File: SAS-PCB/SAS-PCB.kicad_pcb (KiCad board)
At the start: 2 copper layers, 164 x 88 mm, 23 parts, among them J1-BMP280 Conn_01x06_Pin, J2 Conn_02x20_Odd_Even, J3-GPS1 Conn_01x04_Socket, J4-LCD1 Conn_01x04_Socket, J4-LCD2 Conn_01x04_Socket, J5_Batt1 691137710002

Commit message: Rooting terminé
Reste à refaire les mounting holes et enlever les bouttes de cuivre trop mince.
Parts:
- removed Fan_1, Fan_2: 691137710002, SAS-Librarie-Empreinte:bornie_2position
- added J8-Fan1: Conn_01x04_Socket, SAS-Librarie-Empreinte:Conn_4_pos, F.Cu at (182.1, 52.2)
- added J9-Fan2: Conn_01x04_Socket, SAS-Librarie-Empreinte:Conn_4_pos, F.Cu at (182.1, 36.8)
- J4-BMP280: renamed from J1-BMP280; footprint SAS-Librarie-Empreinte:Conn_6_pos -> SAS-Librarie-Empreinte:Header-BMP280
- J5-GPS1: renamed from J3-GPS1; footprint SAS-Librarie-Empreinte:Conn_4_pos -> SAS-Librarie-Empreinte:conn-GPS
- moved Bouton_6 122.4 mm to (134.0, 109.5), turned to 180 degrees
- moved J4-BMP280 114.0 mm to (144.5, 68.9), turned to 180 degrees
- moved J3-LCD2 103.6 mm to (191.2, 82.3)
- moved Bouton_5 99.6 mm to (145.5, 109.5), turned to 180 degrees
- moved R6 98.7 mm to (141.3, 102.5), turned to 90 degrees
- moved Bouton_1 94.9 mm to (191.5, 109.5), turned to 180 degrees
- moved Bouton_4 83.6 mm to (157.0, 109.5), turned to 180 degrees
- moved R1 81.6 mm to (194.0, 97.5), turned to -90 degrees
- moved J1_Batt1 81.6 mm to (203.0, 62.5), turned to 90 degrees
- moved Bouton_2 79.5 mm to (180.0, 109.5), turned to 180 degrees
- moved J5-GPS1 77.4 mm to (143.5, 49.0), turned to 180 degrees
- moved Bouton_3 75.8 mm to (168.5, 109.5), turned to 180 degrees
- moved R5 74.9 mm to (152.8, 102.5), turned to 90 degrees
- moved R7 71.2 mm to (165.2, 68.0), turned to -90 degrees
- moved J2-LCD1 66.6 mm to (172.8, 82.3)
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- renumbered J5_Batt1 to J1_Batt1, J4-LCD1 to J2-LCD1, J4-LCD2 to J3-LCD2, J2 to J6-cable-plat1, RFD900x1 to J7-RFD900x1
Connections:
- J6-cable-plat1 pad 12: unconnected-(J2-Pin_12-Pad12) -> Fan1_PWM
- J6-cable-plat1 pad 13: unconnected-(J2-Pin_13-Pad13) -> Fan2_PWM
- J6-cable-plat1 pad 22: unconnected-(J2-Pin_22-Pad22) -> Fan1_RPM
- J6-cable-plat1 pad 24: unconnected-(J2-Pin_24-Pad24) -> Fan2_RPM
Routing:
- net Fan2_RPM: track 0.00 -> 115.2 mm
- net Fan1_RPM: track 0.00 -> 110.9 mm
- net Fan1_PWM: track 0.00 -> 93.0 mm
- net SDA: track 0.00 -> 90.3 mm
- net SCL: track 0.00 -> 88.8 mm
- net Bouton_1: track 0.00 -> 72.4 mm
- net Fan2_PWM: track 0.00 -> 62.7 mm
- net Bouton_2: track 0.00 -> 59.9 mm
- net Bouton_3: track 0.00 -> 47.0 mm
- net RXD: track 0.00 -> 41.5 mm
- net TXD: track 0.00 -> 37.5 mm
- net Bouton_4: track 0.00 -> 34.5 mm
- net Bouton_5: track 0.00 -> 21.9 mm
- net Bouton_6: track 0.00 -> 9.39 mm
- net Net-(Bouton_5-GND): track 0.00 -> 7.87 mm
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- added copper zone on F.Cu, net +3.3V
- added copper zone on F.Cu, net +5V
- added copper zone on B.Cu, net GND
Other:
- board size 164 x 88 mm -> 96.5 x 85.5 mm
- board text added: "GAUL-SAS"

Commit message: Header Fix
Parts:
- moved J4-BMP280 1.57 mm to (144.5, 67.3)
- moved R4 0.30 mm to (164.6, 102.5)
- moved R3 0.23 mm to (176.0, 102.5)
- moved R6 0.18 mm to (141.5, 102.5)
- moved R2 0.13 mm to (182.4, 97.5)
- moved R5 0.11 mm to (152.9, 102.5)
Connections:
- J6-cable-plat1 pad 11: unconnected-(J6-cable-plat1-Pin_11-Pad11) -> Bouton_1
- J6-cable-plat1 pad 12: Fan1_PWM -> unconnected-(J6-cable-plat1-Pin_12-Pad12)
- J6-cable-plat1 pad 13: Fan2_PWM -> Bouton_2
- J6-cable-plat1 pad 15: unconnected-(J6-cable-plat1-Pin_15-Pad15) -> Bouton_3
- J6-cable-plat1 pad 16: unconnected-(J6-cable-plat1-Pin_16-Pad16) -> Fan1_RPM
- J6-cable-plat1 pad 18: unconnected-(J6-cable-plat1-Pin_18-Pad18) -> Fan2_RPM
- J6-cable-plat1 pad 22: Fan1_RPM -> unconnected-(J6-cable-plat1-Pin_22-Pad22)
- J6-cable-plat1 pad 24: Fan2_RPM -> unconnected-(J6-cable-plat1-Pin_24-Pad24)
- J6-cable-plat1 pad 27: Bouton_1 -> unconnected-(J6-cable-plat1-Pin_27-Pad27)
- J6-cable-plat1 pad 29: Bouton_2 -> Bouton_4
- J6-cable-plat1 pad 31: Bouton_3 -> Bouton_5
- J6-cable-plat1 pad 32: unconnected-(J6-cable-plat1-Pin_32-Pad32) -> Fan1_PWM
- J6-cable-plat1 pad 33: Bouton_4 -> Fan2_PWM
- J6-cable-plat1 pad 35: Bouton_5 -> unconnected-(J6-cable-plat1-Pin_35-Pad35)
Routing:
- net +3.3V: track 0.00 -> 35.4 mm
- net Bouton_1: track 72.4 -> 91.6 mm
- net Bouton_2: track 59.9 -> 78.7 mm
- net Bouton_3: track 47.0 -> 65.8 mm
- net Fan2_PWM: track 62.7 -> 80.8 mm
- net Fan1_PWM: track 93.0 -> 105.5 mm
- net Fan1_RPM: track 110.9 -> 102.8 mm
- net Fan2_RPM: track 115.2 -> 107.5 mm
- net Bouton_4: track 34.5 -> 36.8 mm
- net Bouton_5: track 21.9 -> 24.0 mm
- net RXD: track 41.5 -> 42.6 mm

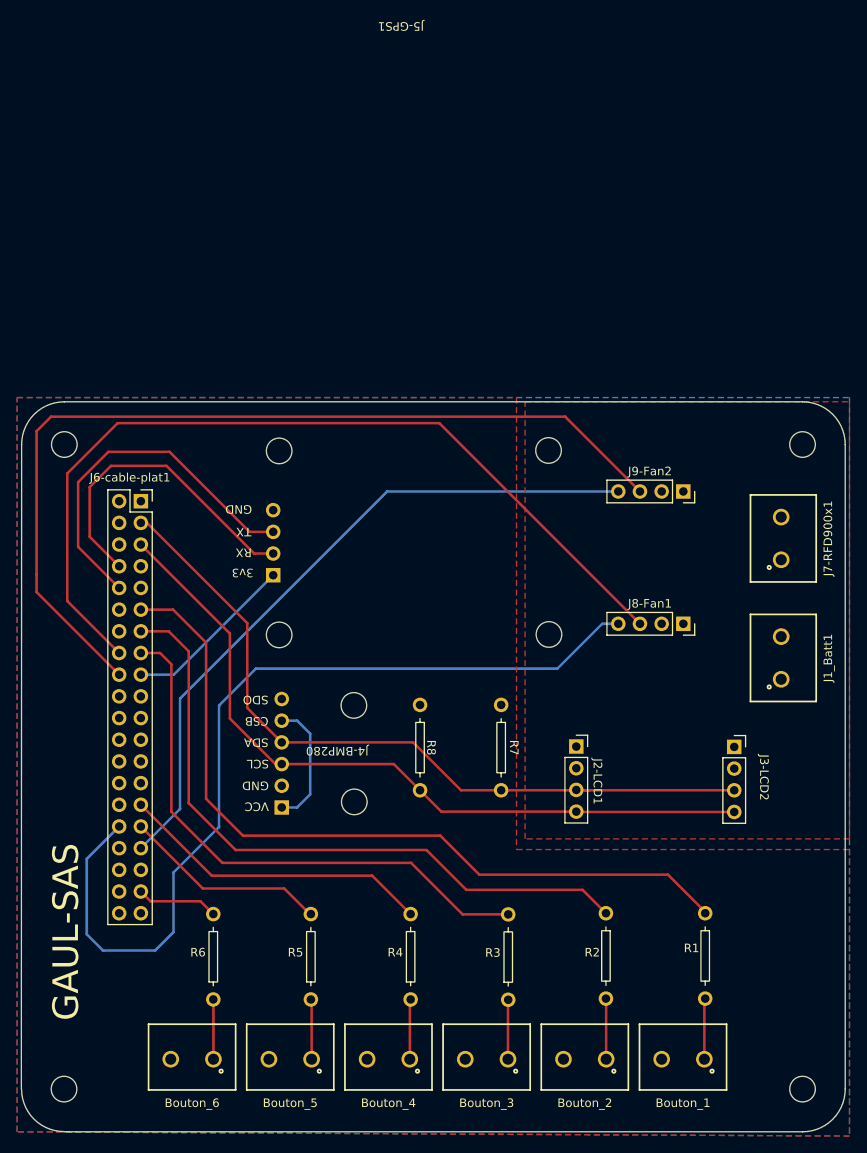
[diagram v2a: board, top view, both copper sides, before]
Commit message: Modification des power plane, corrections DRC et extraction des fichiers gerber
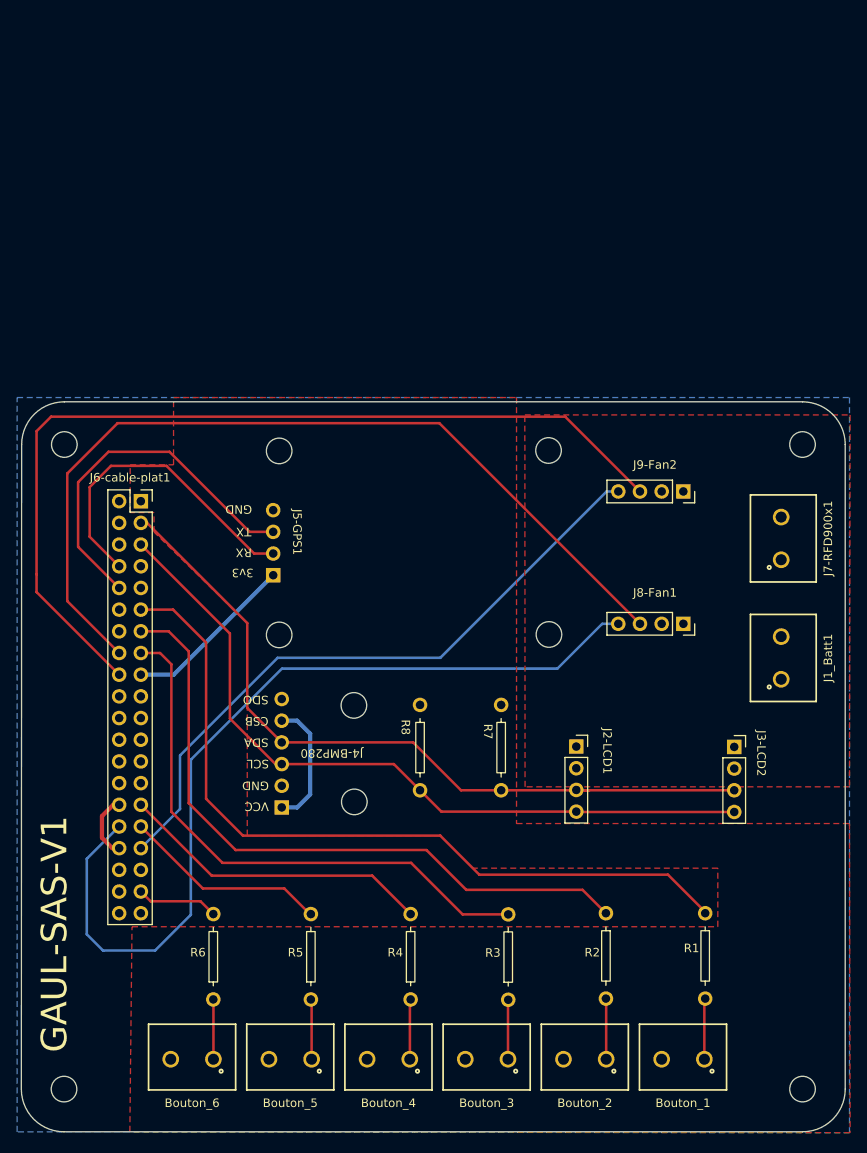
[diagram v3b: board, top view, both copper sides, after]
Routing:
- net GND: track 0.00 -> 7.62 mm
- net Fan2_PWM: track 80.8 -> 76.9 mm
- net Fan1_PWM: track 105.5 -> 103.7 mm
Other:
- board text added: "GAUL-SAS-V1"
- board text removed: "GAUL-SAS"
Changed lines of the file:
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@@
 			(outputformat 1)
 			(mirror no)
-			(drillshape 1)
+			(drillshape 0)
 			(scaleselection 1)
-			(outputdirectory "")
+			(outputdirectory "./")
 		)
 	)
@@
 		(at 143.5 49 180)
 		(property "Reference" "J5-GPS1"
-			(at -14.96 60.5 180)
+			(at -2.804 1.248 -90)
 			(unlocked yes)
 			(layer "F.SilkS")
@@
 			)
 		)
-		(fp_text user "${REFERENCE}"
-			(at -14.96 63.5 180)
-			(unlocked yes)
-			(layer "F.Fab")
-			(effects
-				(font
-					(size 1 1)
-					(thickness 0.15)
-				)
-			)
-		)
 		(pad "1" thru_hole rect
 			(at 0 -3.81 180)
@@
 		(at 172.75 82.28)
 		(property "Reference" "J2-LCD1"
-			(at 8.75 -5.32 -90)
+			(at 9.876 -8.874 -90)
 			(unlocked yes)
 			(layer "F.SilkS")
@@
 		(at 165.2 68 -90)
 		(property "Reference" "R7"
-			(at 5 -6.5 -90)
+			(at 3.12 -3.456 -90)
 			(unlocked yes)
 			(layer "F.SilkS")
@@
 		(at 144.5 67.31 180)
 		(property "Reference" "J4-BMP280"
-			(at -6.5 -6.08 180)
+			(at -5.868 -6.35 180)
 			(unlocked yes)
 			(layer "F.SilkS")
@@
 		(at 191.25 82.32)
 		(property "Reference" "J3-LCD2"
-			(at 9.75 -5.82 -90)
+			(at 9.41 -8.66 -90)
 			(unlocked yes)
 			(layer "F.SilkS")
@@
 		(at 155.7 68 -90)
 		(property "Reference" "R8"
-			(at 5 -6.3 -90)
+			(at 2.612 -3.304 -90)
 			(unlocked yes)
 			(layer "F.SilkS")
@@
 		(at 182.14 36.75 -90)
 		(property "Reference" "J9-Fan2"
-			(at 3.8875 -5.4875 0)
+			(at 3.128 -6.074 0)
 			(unlocked yes)
 			(layer "F.SilkS")
@@
 		(at 182.14 52.25 -90)
 		(property "Reference" "J8-Fan1"
-			(at 3.8875 -5.4875 0)
+			(at 2.614 -6.074 0)
 			(unlocked yes)
 			(layer "F.SilkS")
@@
 	)
 	(gr_arc
-		(start 119 117.974937)
-		(mid 115.482188 116.517812)
-		(end 114.025063 113)
+		(start 119 118)
+		(mid 115.464466 116.535534)
+		(end 114 113)
 		(stroke
 			(width 0.05)
@@
 		(stroke
 			(width 0.05)
-			(type default)
+			(type solid)
 		)
 		(fill none)
@@
 		(layer "Edge.Cuts")
 	)
-	(gr_text "GAUL-SAS"
-		(at 121 105 90)
+	(gr_text "GAUL-SAS-V1"
+		(at 119.634 108.712 90)
 		(layer "F.SilkS")
 		(effects
 			(font
 				(size 3 3)
-				(thickness 0.1)
+				(thickness 0.3)
 			)
 			(justify left bottom)
@@
 		(start 147.828 71.374)
 		(end 146.304 69.85)
-		(width 0.3)
+		(width 0.5)
 		(layer "B.Cu")
 		(net 2)
@@
 		(start 146.304 80.01)
 		(end 147.828 78.486)
-		(width 0.3)
+		(width 0.5)
 		(layer "B.Cu")
 		(net 2)
@@
 		(start 144.5 80.01)
 		(end 146.304 80.01)
-		(width 0.3)
+		(width 0.5)
 		(layer "B.Cu")
 		(net 2)
@@
 		(start 147.828 78.486)
 		(end 147.828 71.374)
-		(width 0.3)
+		(width 0.5)
 		(layer "B.Cu")
 		(net 2)
@@
 		(start 146.304 69.85)
 		(end 144.5 69.85)
-		(width 0.3)
+		(width 0.5)
 		(layer "B.Cu")
 		(net 2)
@@
 		(start 131.85 64.46)
 		(end 143.5 52.81)
-		(width 0.3)
+		(width 0.5)
 		(layer "B.Cu")
 		(net 2)
@@
 		(start 128 64.46)
 		(end 131.85 64.46)
-		(width 0.3)
+		(width 0.5)
 		(layer "B.Cu")
 		(net 2)
@@
 	)
 	(segment
+		(start 123.444 81.026)
+		(end 124.77 79.7)
+		(width 0.5)
+		(layer "F.Cu")
+		(net 9)
+	)
+	(segment
+		(start 124.77 79.7)
+		(end 125.46 79.7)
+		(width 0.5)
+		(layer "F.Cu")
+		(net 9)
+	)
+	(segment
+		(start 125.46 84.78)
+		(end 124.658 84.78)
+		(width 0.5)
+		(layer "F.Cu")
+		(net 9)
+	)
+	(segment
+		(start 124.658 84.78)
+		(end 123.444 83.566)
+		(width 0.5)
+		(layer "F.Cu")
+		(net 9)
+	)
+	(segment
+		(start 123.444 83.566)
+		(end 123.444 81.026)
+		(width 0.5)
+		(layer "F.Cu")
+		(net 9)
+	)
+	(segment
 		(start 144.5 74.93)
 		(end 143.764 74.93)
@@
 	)
 	(segment
-		(start 132.588 67.263585)
-		(end 132.588 80.192)
+		(start 183.92 43)
+		(end 182.552 43)
 		(width 0.3)
 		(layer "B.Cu")
@@
 	)
 	(segment
-		(start 141.019877 58.831708)
-		(end 132.588 67.263585)
+		(start 132.588 80.192)
+		(end 128 84.78)
 		(width 0.3)
 		(layer "B.Cu")
@@
 	)
 	(segment
-		(start 156.851584 43)
-		(end 141.019877 58.831708)
+		(start 132.588 73.914)
+		(end 132.588 80.192)
 		(width 0.3)
 		(layer "B.Cu")
@@
 	)
 	(segment
-		(start 183.92 43)
-		(end 156.851584 43)
+		(start 144.018 62.484)
+		(end 132.588 73.914)
 		(width 0.3)
 		(layer "B.Cu")
@@
 	)
 	(segment
-		(start 132.588 80.192)
-		(end 128 84.78)
+		(start 163.068 62.484)
+		(end 144.018 62.484)
+		(width 0.3)
+		(layer "B.Cu")
+		(net 18)
+	)
+	(segment
+		(start 182.552 43)
+		(end 163.068 62.484)
 		(width 0.3)
 		(layer "B.Cu")
@@
 	)
 	(segment
-		(start 183.92 58.5)
-		(end 182.038 58.5)
-		(width 0.3)
-		(layer "B.Cu")
-		(net 22)
-	)
-	(segment
-		(start 129.667 96.774)
-		(end 123.571 96.774)
+		(start 182.038 58.5)
+		(end 176.784 63.754)
 		(width 0.3)
 		(layer "B.Cu")
@@
 	)
 	(segment
-		(start 176.784 63.754)
-		(end 141.478 63.754)
+		(start 144.526 63.754)
+		(end 133.858 74.422)
 		(width 0.3)
 		(layer "B.Cu")
@@
 	)
 	(segment
-		(start 137.16 68.072)
-		(end 137.16 82.296)
-		(width 0.3)
-		(layer "B.Cu")
-		(net 22)
-	)
-	(segment
-		(start 141.478 63.754)
-		(end 137.16 68.072)
+		(start 129.667 96.774)
+		(end 123.571 96.774)
 		(width 0.3)
 		(layer "B.Cu")
@@
 	)
 	(segment
-		(start 182.038 58.5)
-		(end 176.784 63.754)
+		(start 183.92 58.5)
+		(end 182.038 58.5)
 		(width 0.3)
 		(layer "B.Cu")
@@
 	)
 	(segment
-		(start 121.666 94.869)
-		(end 121.666 86.034)
+		(start 121.666 86.034)
+		(end 125.46 82.24)
 		(width 0.3)
 		(layer "B.Cu")
@@
 	)
 	(segment
-		(start 121.666 86.034)
-		(end 125.46 82.24)
+		(start 133.858 92.583)
+		(end 129.667 96.774)
 		(width 0.3)
 		(layer "B.Cu")
@@
 	)
 	(segment
-		(start 137.16 82.296)
-		(end 131.826 87.63)
+		(start 121.666 94.869)
+		(end 121.666 86.034)
 		(width 0.3)
 		(layer "B.Cu")
@@
 	)
 	(segment
-		(start 131.826 87.63)
-		(end 131.826 94.615)
+		(start 133.858 74.422)
+		(end 133.858 92.583)
 		(width 0.3)
 		(layer "B.Cu")
@@
 	)
 	(segment
-		(start 131.826 94.615)
-		(end 129.667 96.774)
+		(start 176.784 63.754)
+		(end 144.526 63.754)
 		(width 0.3)
 		(layer "B.Cu")
@@
 		(polygon
 			(pts
-				(xy 113.5 118) (xy 113.5 32) (xy 172 32) (xy 172 84.944) (xy 211 84.944) (xy 211 118.5)
+				(xy 126.708 118) (xy 126.962 93.98) (xy 140.462 93.98) (xy 195.58 93.98) (xy 195.58 87.122) (xy 166.878 87.122)
+				(xy 163.068 83.312) (xy 140.462 83.312) (xy 140.462 58.42) (xy 129.54 47.752) (xy 129.54 45.466)
+				(xy 126.746 45.466) (xy 126.746 39.878) (xy 131.826 39.878) (xy 131.826 32) (xy 172 32) (xy 172 81.896)
+				(xy 211 81.896) (xy 211.074 118.11)
 			)
 		)
@@
 		(polygon
 			(pts
-				(xy 211 32.5) (xy 211 83.69) (xy 173 83.69) (xy 173 32.5)
+				(xy 211.074 34.036) (xy 211 77.594) (xy 173 77.594) (xy 172.974 34.036)
 			)
 		)
@@
 		(polygon
 			(pts
-				(xy 113.5 32) (xy 211 32) (xy 211 118.5) (xy 113.5 118)
+				(xy 113.5 32) (xy 211 32) (xy 211 118.11) (xy 113.5 118)
 			)
 		)

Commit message: u1
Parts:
- J1_Batt1, J7-RFD900x1: footprint SAS-Librarie-Empreinte:bornie_2position -> SAS-Librarie-Empreinte:AMASS_XT30U-F_1x02_P5.0mm_Vertical
- moved J9-Fan2 143.7 mm to (58.6, 110.2), turned to 0 degrees
- moved J7-RFD900x1 141.0 mm to (65.7, 80.5)
- moved J8-Fan1 131.5 mm to (58.6, 97.2), turned to 0 degrees
- moved R1 122.6 mm to (73.0, 78.0), turned to 90 degrees
- moved R2 106.2 mm to (78.0, 78.0), turned to 90 degrees
- moved R3 96.2 mm to (83.0, 78.0)
- moved J6-cable-plat1 88.3 mm to (74.2, 114.2), turned to 90 degrees
- moved J1_Batt1 81.0 mm to (134.3, 105.4)
- moved J5-GPS1 80.5 mm to (79.5, 98.0)
- moved R4 80.4 mm to (88.0, 78.0)
- moved Bouton_1 79.3 mm to (125.5, 65.5)
- moved Bouton_2 78.2 mm to (115.3, 65.5)
- moved Bouton_3 77.2 mm to (105.1, 65.5)
- moved Bouton_4 76.1 mm to (94.9, 65.5)
- moved Bouton_5 75.1 mm to (84.7, 65.5)
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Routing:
- net Fan2_RPM: track 107.5 -> 0.00 mm
- net Fan1_PWM: track 103.7 -> 0.00 mm
- net Fan1_RPM: track 102.8 -> 0.00 mm
- net Bouton_1: track 91.6 -> 0.00 mm
- net SDA: track 89.8 -> 0.00 mm
- net SCL: track 88.4 -> 0.00 mm
- net Bouton_2: track 78.7 -> 0.00 mm
- net Fan2_PWM: track 76.9 -> 0.00 mm
- net Bouton_3: track 65.8 -> 0.00 mm
- net RXD: track 42.6 -> 0.00 mm
- net TXD: track 37.5 -> 0.00 mm
- net Bouton_4: track 36.8 -> 0.00 mm
- net +3.3V: track 35.4 -> 0.00 mm
- net Bouton_5: track 24.0 -> 0.00 mm
- net Bouton_6: track 9.58 -> 0.00 mm
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- removed copper zone on F.Cu, net +3.3V
- removed copper zone on F.Cu, net +5V
- removed copper zone on B.Cu, net GND
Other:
- board size 96.5 x 85.5 mm -> 80 x 60 mm
- board text removed: "GAUL-SAS-V1"

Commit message: U2
trial 2
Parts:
- added J10-FTDI1: Conn_01x06, SAS-Librarie-Empreinte:Conn_6_pos, F.Cu at (65.4, 129.0)
- added J11-Conn_RFD900: Conn_01x08, SAS-Librarie-Empreinte:Conn_8_pos, F.Cu at (131.4, 120.7)
- moved J7-RFD900x1 77.6 mm to (130.4, 123.3), turned to 180 degrees
- moved J1_Batt1 69.4 mm to (64.9, 104.0), turned to 0 degrees
- moved J2-LCD1 68.4 mm to (59.9, 84.1)
- moved J9-Fan2 68.2 mm to (125.0, 94.6)
- moved J8-Fan1 68.2 mm to (125.2, 82.7)
- moved J3-LCD2 56.6 mm to (72.0, 87.2), turned to 180 degrees
- moved Bouton_1 51.8 mm to (73.7, 66.4), turned to 0 degrees
- moved Bouton_6 49.2 mm to (123.7, 66.4), turned to 0 degrees
- moved J4-BMP280 42.2 mm to (91.8, 117.9)
- moved J5-GPS1 36.3 mm to (114.2, 87.4), turned to 0 degrees
- moved Bouton_2 31.6 mm to (83.7, 66.4), turned to 0 degrees
- moved Bouton_5 29.0 mm to (113.7, 66.4), turned to 0 degrees
- moved J6-cable-plat1 16.9 mm to (75.3, 131.1)
- moved Bouton_3 11.4 mm to (93.7, 66.4), turned to 0 degrees
- moved R1 9.86 mm to (78.1, 86.5)
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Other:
- board size 80 x 60 mm -> 76.2 x 76.2 mm

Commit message: Version_a_amiliorer
pas tant fonctionnel
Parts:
- removed J11-Conn_RFD900: Conn_01x08, SAS-Librarie-Empreinte:Conn_8_pos
- added J10-FTDI2: Conn_01x06, SAS-Librarie-Empreinte:Conn_6_pos, F.Cu at (124.8, 92.5)
- moved J10-FTDI1 75.8 mm to (131.9, 92.5)
- moved J8-Fan1 31.9 mm to (120.3, 114.2), turned to 90 degrees
- moved J9-Fan2 29.9 mm to (124.8, 124.5)
- moved R7 29.1 mm to (73.0, 86.4), turned to -90 degrees
- moved R8 28.8 mm to (77.3, 86.3), turned to -90 degrees
- moved J7-RFD900x1 25.9 mm to (131.2, 97.5)
- moved J3-LCD2 19.6 mm to (62.4, 104.3), turned to 0 degrees
- moved J4-BMP280 16.5 mm to (75.3, 116.8)
- moved J1_Batt1 12.5 mm to (65.6, 116.5), turned to 90 degrees
- moved R6 10.4 mm to (107.4, 91.0), turned to -90 degrees
- moved R5 8.97 mm to (101.8, 91.0), turned to -90 degrees
- moved R4 8.18 mm to (96.8, 91.0), turned to -90 degrees
- moved R3 7.62 mm to (92.2, 91.0), turned to -90 degrees
- moved R2 7.08 mm to (87.5, 91.0)
- moved J6-cable-plat1 6.99 mm to (75.0, 124.1)
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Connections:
- J10-FTDI1 pad 3: +5V -> unconnected-(J10-FTDI1-Pin_3-Pad3)
- J10-FTDI1 pad 4: RFD_TX -> RFD_RX
- J10-FTDI1 pad 5: RFD_RX -> RFD_TX
- J6-cable-plat1 pad 16: Fan1_RPM -> Fan2_RPM
- J6-cable-plat1 pad 18: Fan2_RPM -> Fan1_RPM
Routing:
- net +3.3V: track 0.00 -> 213.5 mm
- net TXD: track 0.00 -> 149.4 mm
- net RXD: track 0.00 -> 98.4 mm
- net SCL: track 0.00 -> 86.8 mm
- net Fan2_PWM: track 0.00 -> 86.4 mm
- net +5V: track 0.00 -> 75.9 mm
- net Fan1_RPM: track 0.00 -> 71.8 mm
- net SDA: track 0.00 -> 63.9 mm
- net Fan2_RPM: track 0.00 -> 55.2 mm
- net GND: track 0.00 -> 46.7 mm
- net Bouton_6: track 0.00 -> 40.5 mm
- net Fan1_PWM: track 0.00 -> 38.1 mm
- net Bouton_5: track 0.00 -> 37.0 mm
- net Bouton_4: track 0.00 -> 33.8 mm
- net Net-(Bouton_1-GND): track 0.00 -> 32.7 mm
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- added copper zone on B.Cu, net GND
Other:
- outline, holes or cut-outs redrawn
- board text added: "+5V"
- board text added: "2"
- board text added: "21"
- board text added: "3.3V"
- board text added: "3v3"
- board text added: "40"
- board text added: "5V"
- board text added: "B1"
- board text added: "B2"
- board text added: "B3"
- board text added: "B4"
- board text added: "B5"
- board text added: "B6"
- board text added: "BMP"
- board text added: "Batt1"
- board text added: "BattRFD"
- board text added: "CSB"
- board text added: "CTS"
- board text added: "FTDI"
- board text added: "Fan1"
- board text added: "Fan2"
- board text added: "GAUL-SAS-V2-2025"
- board text added: "GND"
- board text added: "GPIO"
- board text added: "GPS"
- board text added: "LCD1"
- board text added: "LCD2"
- board text added: "PMW"
- board text added: "R1"
- board text added: "R2"
- board text added: "R3"
- board text added: "R4"
- board text added: "R5"
- board text added: "R6"
- board text added: "R7"
- board text added: "R8"
- board text added: "RFD"
- board text added: "RPM"
- board text added: "RTS"
- board text added: "RX"
- board text added: "SCL"
- board text added: "SDA"
- board text added: "SDD"
- board text added: "TX"
